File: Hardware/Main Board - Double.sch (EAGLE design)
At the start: 71 parts, among them J1 MICROMOD-2222-C, J10 MICRO-SD-PUSH-PUSH-EXT-PIN, J2 Vertical Qwiic Connector, J4 QWIIC_RIGHT_ANGLE, J5 CORTEX_JTAG_DEBUG_MINIMUM_PTH, J6 MICROMOD_FUNCTION_MAIN, J7 MICROMOD_FUNCTION_MAIN, Q1 3.1A/30V/105mΩ, U1 STG3856QTR, U2 MCP73831, U5 AP7361C-33

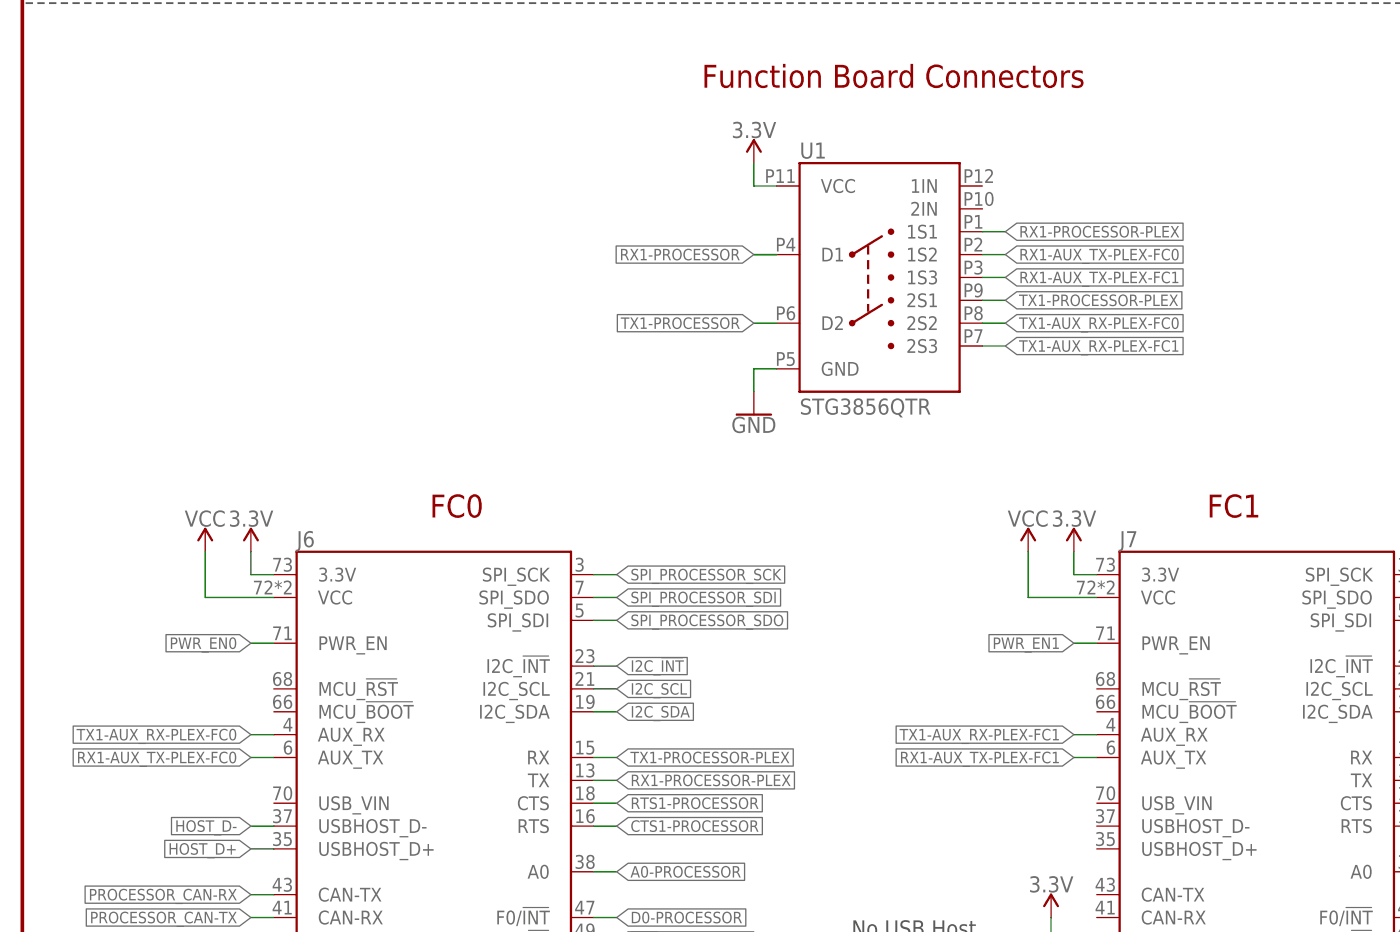
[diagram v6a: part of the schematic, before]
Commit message: Updates the symbol for the multiplexer and net names
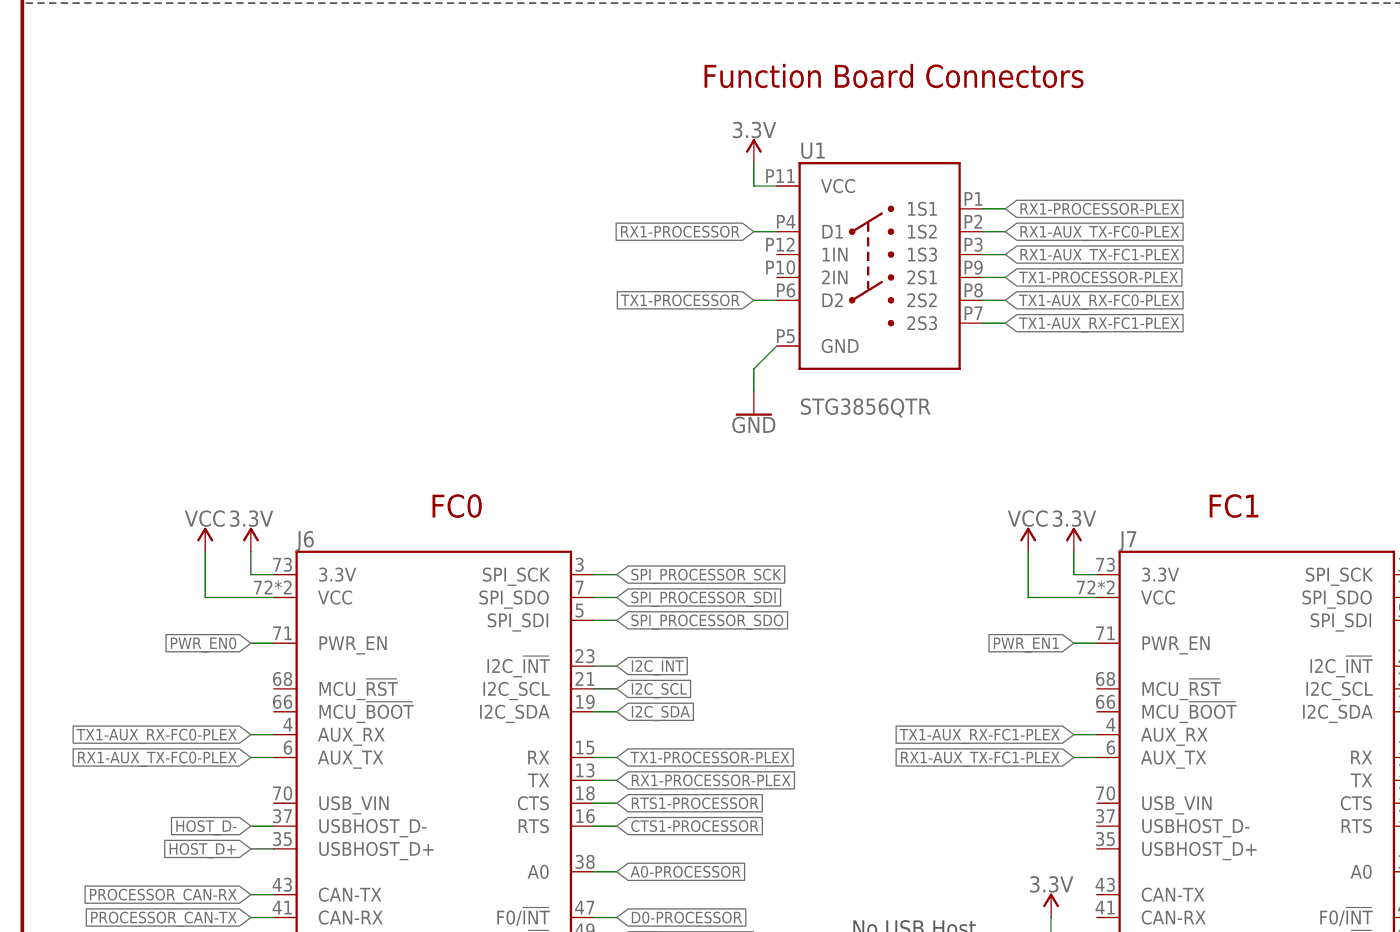
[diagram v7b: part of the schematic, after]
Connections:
- net RX1-AUX_TX-PLEX-FC0 renamed RX1-AUX_TX-FC0-PLEX
- net RX1-AUX_TX-PLEX-FC1 renamed RX1-AUX_TX-FC1-PLEX
- net TX1-AUX_RX-PLEX-FC0 renamed TX1-AUX_RX-FC0-PLEX
- net TX1-AUX_RX-PLEX-FC1 renamed TX1-AUX_RX-FC1-PLEX
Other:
- moved on the sheet: U1
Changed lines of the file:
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@@
 <segment>
 <pinref part="U1" gate="G$1" pin="GND"/>
-<wire x1="81.28" y1="91.44" x2="83.82" y2="91.44" width="0.1524" layer="91"/>
+<wire x1="81.28" y1="91.44" x2="83.82" y2="93.98" width="0.1524" layer="91"/>
 <wire x1="81.28" y1="88.9" x2="81.28" y2="91.44" width="0.1524" layer="91"/>
 <pinref part="GND18" gate="1" pin="GND"/>
@@
 <segment>
 <pinref part="U1" gate="G$1" pin="D2"/>
-<wire x1="81.28" y1="96.52" x2="83.82" y2="96.52" width="0.1524" layer="91"/>
-<label x="81.28" y="96.52" size="1.27" layer="95" font="vector" rot="R180" xref="yes"/>
+<wire x1="81.28" y1="99.06" x2="83.82" y2="99.06" width="0.1524" layer="91"/>
+<label x="81.28" y="99.06" size="1.27" layer="95" font="vector" rot="R180" xref="yes"/>
 </segment>
 </net>
@@
 <segment>
 <pinref part="U1" gate="G$1" pin="D1"/>
-<wire x1="81.28" y1="104.14" x2="83.82" y2="104.14" width="0.1524" layer="91"/>
-<wire x1="81.28" y1="104.14" x2="83.82" y2="104.14" width="0.1524" layer="91"/>
-<label x="81.28" y="104.14" size="1.27" layer="95" font="vector" rot="R180" xref="yes"/>
+<wire x1="81.28" y1="106.68" x2="83.82" y2="106.68" width="0.1524" layer="91"/>
+<label x="81.28" y="106.68" size="1.27" layer="95" font="vector" rot="R180" xref="yes"/>
 </segment>
 </net>
@@
 <segment>
 <pinref part="U1" gate="G$1" pin="2S1"/>
-<wire x1="109.22" y1="99.06" x2="106.68" y2="99.06" width="0.1524" layer="91"/>
-<label x="109.22" y="99.06" size="1.27" layer="95" font="vector" xref="yes"/>
+<wire x1="109.22" y1="101.6" x2="106.68" y2="101.6" width="0.1524" layer="91"/>
+<label x="109.22" y="101.6" size="1.27" layer="95" font="vector" xref="yes"/>
 </segment>
 </net>
@@
 <segment>
 <pinref part="U1" gate="G$1" pin="1S1"/>
-<wire x1="109.22" y1="106.68" x2="106.68" y2="106.68" width="0.1524" layer="91"/>
-<label x="109.22" y="106.68" size="1.27" layer="95" font="vector" xref="yes"/>
-</segment>
-</net>
-<net name="TX1-AUX_RX-PLEX-FC0" class="0">
+<wire x1="109.22" y1="109.22" x2="106.68" y2="109.22" width="0.1524" layer="91"/>
+<label x="109.22" y="109.22" size="1.27" layer="95" font="vector" xref="yes"/>
+</segment>
+</net>
+<net name="TX1-AUX_RX-FC0-PLEX" class="0">
 <segment>
 <pinref part="J6" gate="J1" pin="AUX_RX"/>
@@
 <segment>
 <pinref part="U1" gate="G$1" pin="2S2"/>
-<wire x1="109.22" y1="96.52" x2="106.68" y2="96.52" width="0.1524" layer="91"/>
-<label x="109.22" y="96.52" size="1.27" layer="95" font="vector" xref="yes"/>
-</segment>
-</net>
-<net name="RX1-AUX_TX-PLEX-FC1" class="0">
+<wire x1="109.22" y1="99.06" x2="106.68" y2="99.06" width="0.1524" layer="91"/>
+<label x="109.22" y="99.06" size="1.27" layer="95" font="vector" xref="yes"/>
+</segment>
+</net>
+<net name="RX1-AUX_TX-FC1-PLEX" class="0">
 <segment>
 <pinref part="U1" gate="G$1" pin="1S3"/>
-<wire x1="109.22" y1="101.6" x2="106.68" y2="101.6" width="0.1524" layer="91"/>
-<label x="109.22" y="101.6" size="1.27" layer="95" font="vector" xref="yes"/>
+<wire x1="109.22" y1="104.14" x2="106.68" y2="104.14" width="0.1524" layer="91"/>
+<label x="109.22" y="104.14" size="1.27" layer="95" font="vector" xref="yes"/>
 </segment>
 <segment>
@@
 </segment>
 </net>
-<net name="RX1-AUX_TX-PLEX-FC0" class="0">
+<net name="RX1-AUX_TX-FC0-PLEX" class="0">
 <segment>
 <pinref part="J6" gate="J1" pin="AUX_TX"/>
@@
 <segment>
 <pinref part="U1" gate="G$1" pin="1S2"/>
-<wire x1="109.22" y1="104.14" x2="106.68" y2="104.14" width="0.1524" layer="91"/>
-<label x="109.22" y="104.14" size="1.27" layer="95" font="vector" xref="yes"/>
+<wire x1="109.22" y1="106.68" x2="106.68" y2="106.68" width="0.1524" layer="91"/>
+<label x="109.22" y="106.68" size="1.27" layer="95" font="vector" xref="yes"/>
 </segment>
 </net>
@@
 </segment>
 </net>
-<net name="TX1-AUX_RX-PLEX-FC1" class="0">
+<net name="TX1-AUX_RX-FC1-PLEX" class="0">
 <segment>
 <pinref part="U1" gate="G$1" pin="2S3"/>
-<wire x1="109.22" y1="93.98" x2="106.68" y2="93.98" width="0.1524" layer="91"/>
-<label x="109.22" y="93.98" size="1.27" layer="95" font="vector" xref="yes"/>
-</segment>
-<segment>
+<wire x1="109.22" y1="96.52" x2="106.68" y2="96.52" width="0.1524" layer="91"/>
+<label x="109.22" y="96.52" size="1.27" layer="95" font="vector" xref="yes"/>
+</segment>
+<segment>

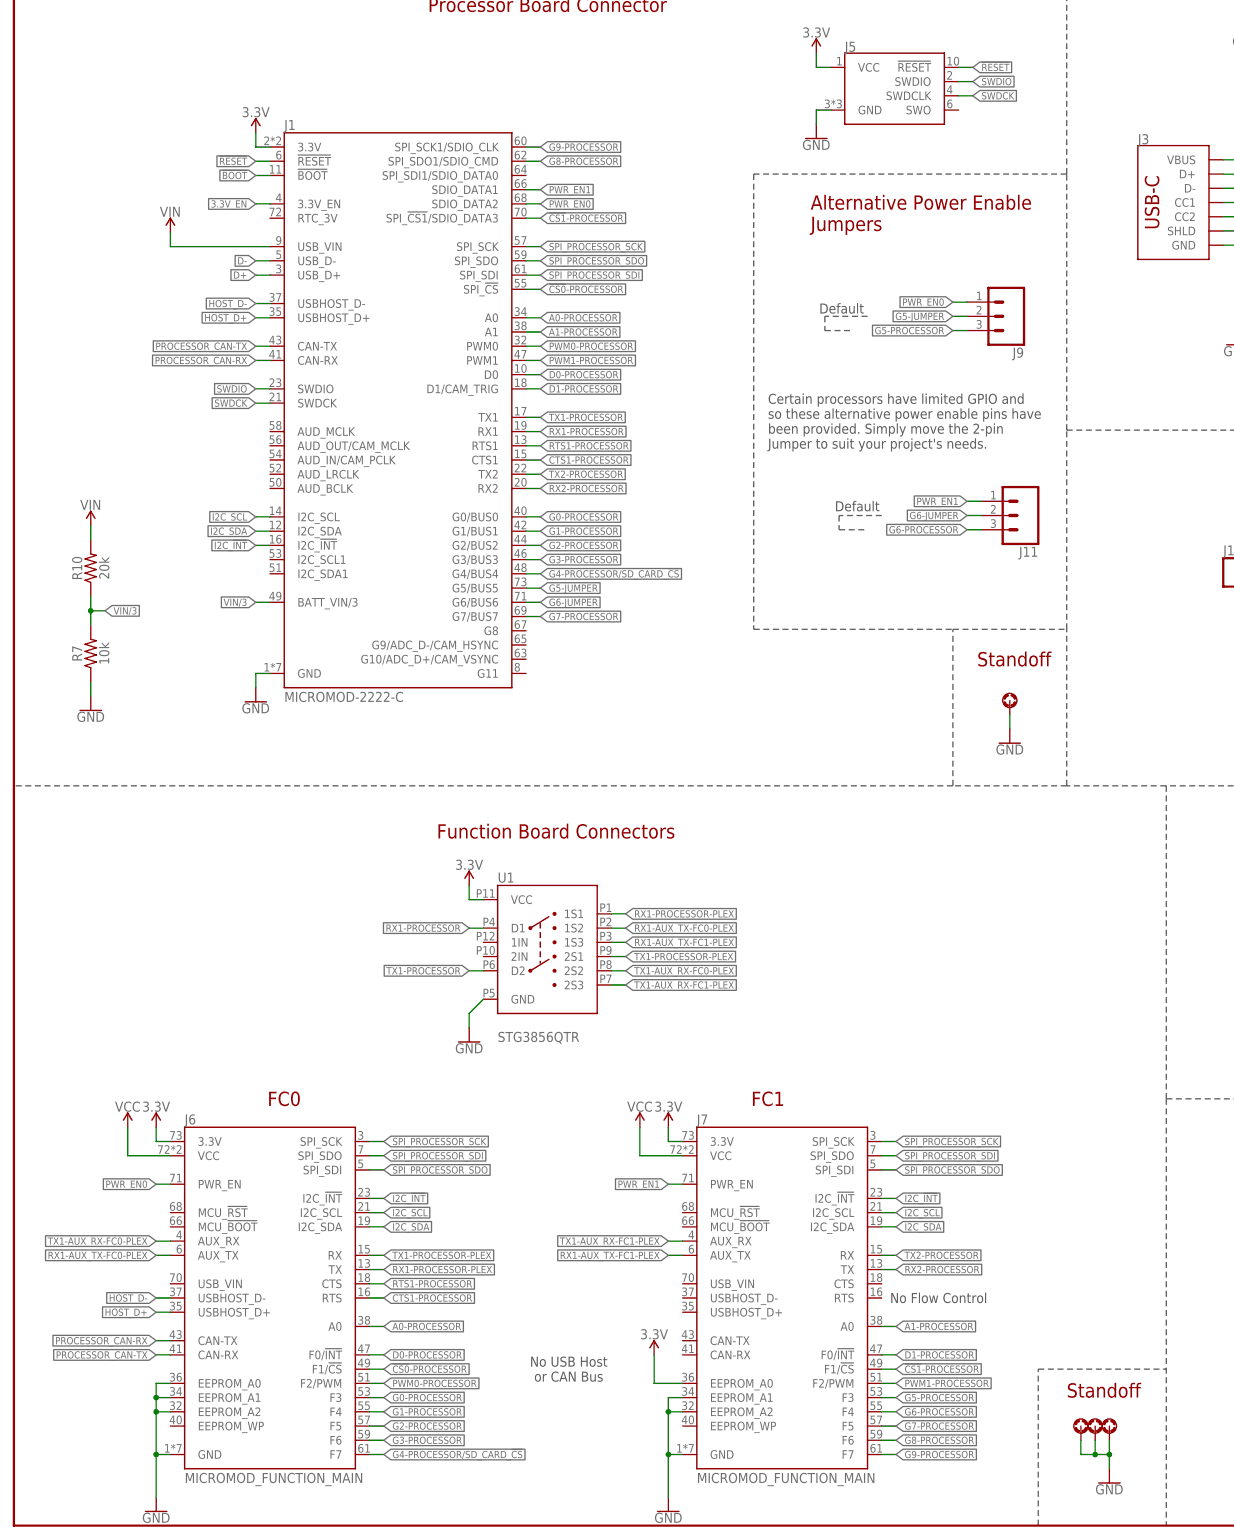
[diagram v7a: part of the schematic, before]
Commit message: Double routes chip select and analog one
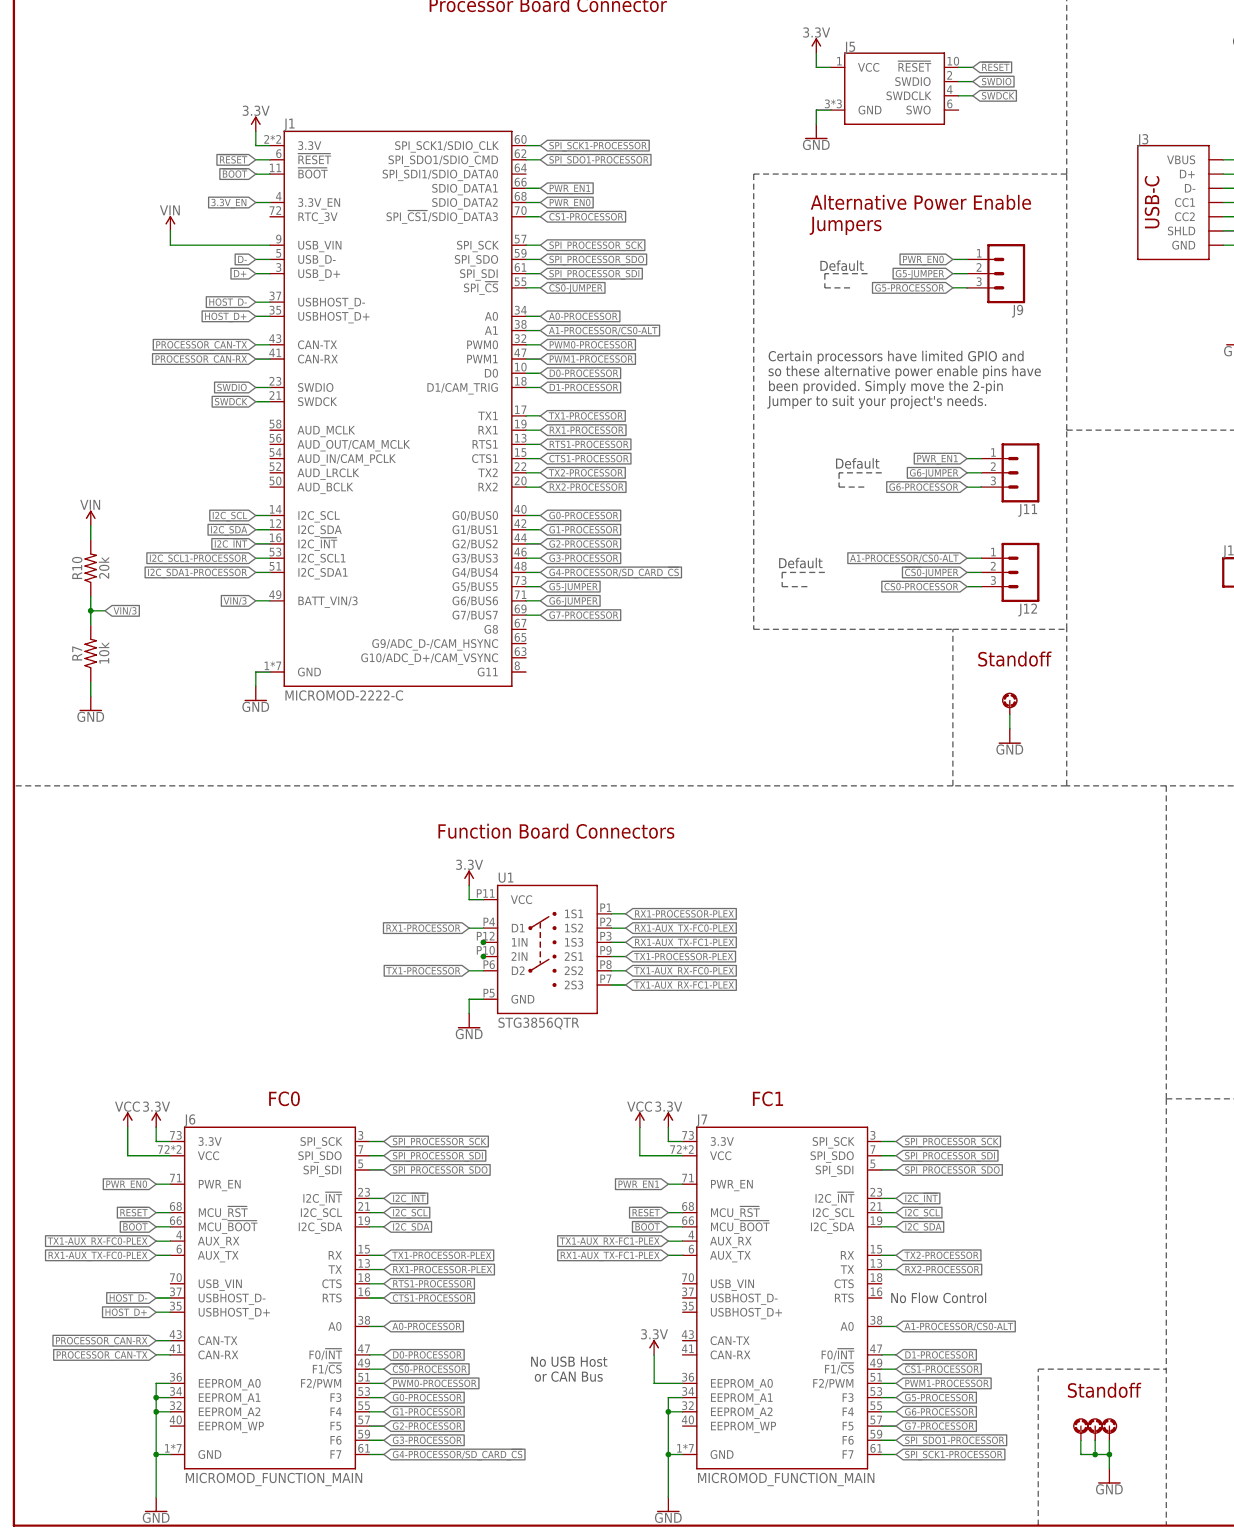
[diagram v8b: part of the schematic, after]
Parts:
- added J12: (no value), SparkFun-Connectors:CONN_03LOCK
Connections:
- net G8-PROCESSOR renamed SPI_SDO1-PROCESSOR
- net G9-PROCESSOR renamed SPI_SCK1-PROCESSOR
- net N$11 renamed SHLD
- removed net A1-PROCESSOR: J1.A1, J7.A0
- new net !CS0!-JUMPER: J1.SPI_!CS!, J12.2
- new net A1-PROCESSOR/CS0-ALT: J1.A1, J12.1, J7.A0
- new net I2C_SCL1-PROCESSOR: J1.I2C_SCL1
- new net I2C_SDA1-PROCESSOR: J1.I2C_SDA1
- net !BOOT!: now also J6.MCU_!BOOT!, J7.MCU_!BOOT!
- net !CS0!-PROCESSOR: now also J12.3; no longer J1.SPI_!CS!
- net !RESET!: now also J6.MCU_!RST!, J7.MCU_!RST!
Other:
- moved on the sheet: J11, J9
